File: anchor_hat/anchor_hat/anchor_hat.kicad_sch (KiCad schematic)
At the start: 25 parts, among them J1 GPIO, J2 Motor 1, J3 Motor 2, J4 24v in barrel jack, J5 24v out slip ring, J7 5v out fan right angle, U2 MCP2515-xST, U3 SN65HVD230, U4 TPS54302, Y1 12M

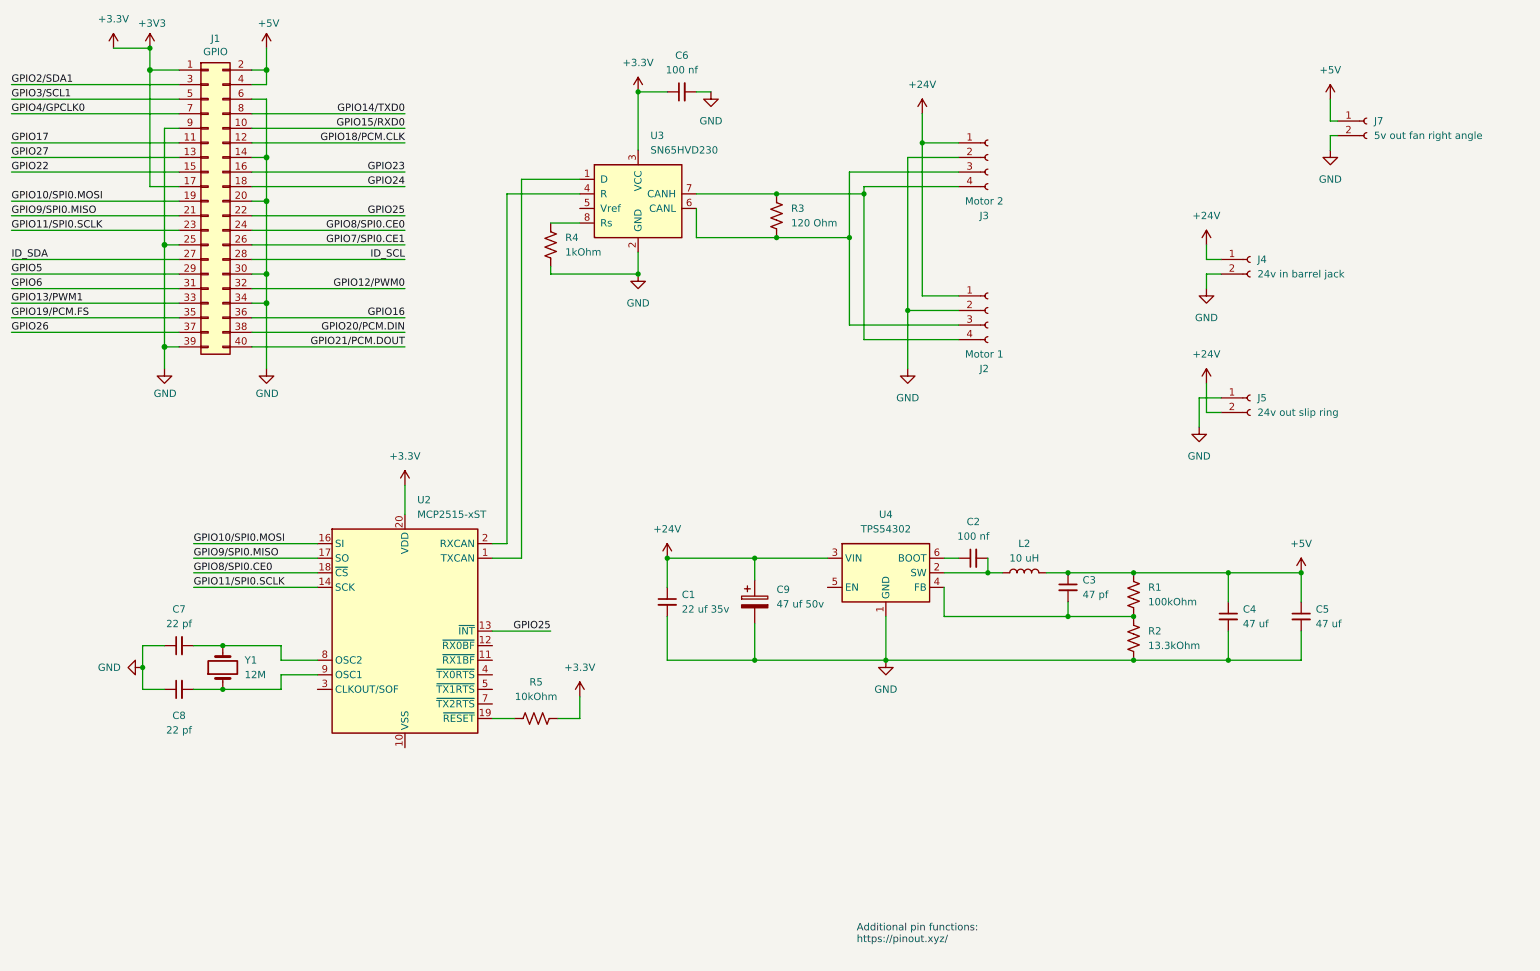
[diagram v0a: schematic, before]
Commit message: anchor hat: tvs clamps, gpio-switchable motor rail, buck uvlo, smaller crystal
TVS diodes on both sides of the buck. D1 (SMAJ26A, C49370) clamps the 24V
input, D2 (SMAJ6.0A, C364284) the 5V output; both unidirectional, cathode to
the rail. D2 is 6.0A rather than 5.0A because R1/R2 against the TPS54302's
0.596V reference put the rail at 5.08V, above an SMAJ5.0A's standoff, which
would leave it leaking continuously.

Motor rail is switchable from GPIO23. Q1 (AOD4185) is a high-side P-FET
feeding a new +24V_MOT net supplying only J2 and J3; J4, J5 and the buck stay
on +24V so the Pi keeps power. Q3 level-shifts the GPIO, R6/R7 clamp Vgs to
about -12V (the FET's limit is +/-20V, and pulling the gate to ground from 24V
would exceed it), and C10 slews the output over ~17ms so inrush into the motor
drivers does not brown out the Pi. R9 holds the switch off while the GPIO is
high-Z, and GPIO23 defaults to pull-down at boot, so the motors stay off until
firmware asserts. R10 is a DNP bleeder: without it the drivers' input caps
have no discharge path and an off-pulse does not actually power cycle them.

R11/R12 raise the buck's UVLO. U4's EN pin was floating, so the internal 4.1V
threshold let back-EMF from hand-spinning the motors boot the Pi. 560k/39k
give VSTART 18.5V and VSTOP 16.6V by the datasheet's equations 1 and 2,
leaving 7.4V of droop margin below nominal.

Y1 moves from an HC-49/U-S through-hole can to a 3225 SMD crystal (C9002).
Same 12MHz and the same 80 ohm ESR, so bit timing and oscillator startup
margin are unchanged, but it frees ~44mm2 and two drills. C7/C8 stay at 22pF:
the 18 to 20pF load change pulls the crystal about 37ppm, against the
MCP2515's 1.7% node-to-node budget.

The PCB and the BOM csv do not reflect any of this yet.

Co-Authored-By: Claude Opus 5 <noreply@anthropic.com>
Claude-Session: https://claude.ai/code/session_011o3vJPykXRkMivW79T9ddF
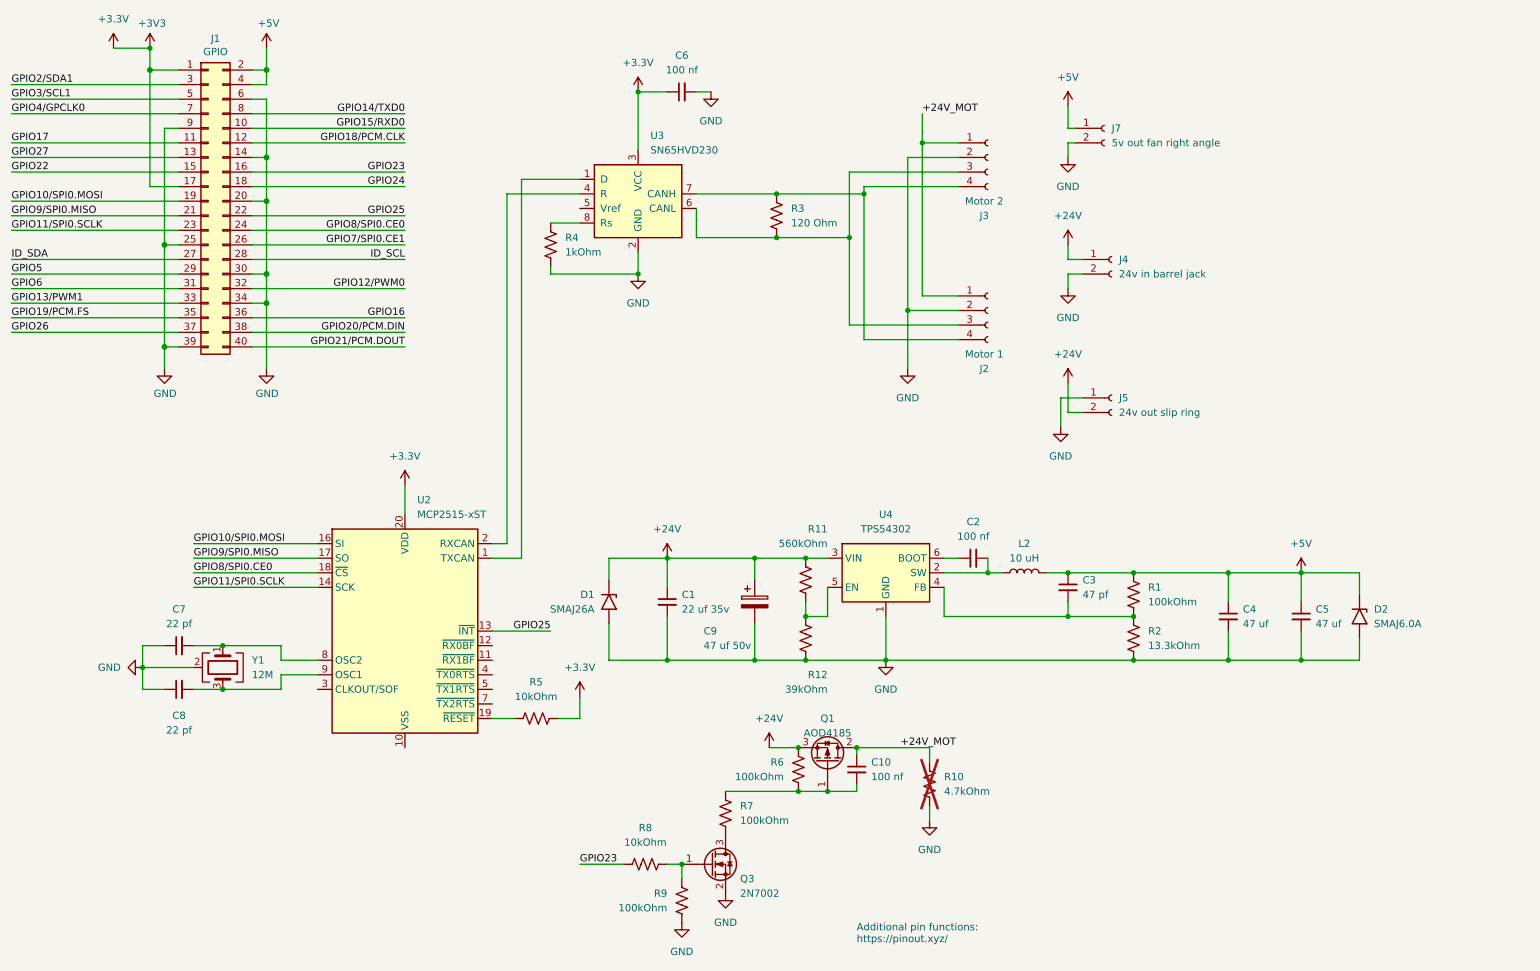
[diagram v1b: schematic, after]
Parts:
- added C10: 100 nf, Capacitor_SMD:C_0603_1608Metric, symbol Device:C_Small
- added D1: SMAJ26A, Diode_SMD:D_SMA, symbol Diode:SMAJ26A
- added D2: SMAJ6.0A, Diode_SMD:D_SMA, symbol Diode:SMAJ6.0A
- added Q1: AOD4185, Package_TO_SOT_SMD:TO-252-2, symbol Transistor_FET:Q_PMOS_GDS
- added Q3: 2N7002, Package_TO_SOT_SMD:SOT-23, symbol Transistor_FET:2N7002
- added R10: 4.7kOhm, Resistor_SMD:R_1206_3216Metric, symbol Device:R_US
- added R11: 560kOhm, Resistor_SMD:R_0603_1608Metric, symbol Device:R_US
- added R12: 39kOhm, Resistor_SMD:R_0603_1608Metric, symbol Device:R_US
- added R6, R7, R9: 100kOhm, Resistor_SMD:R_0603_1608Metric, symbol Device:R_US
- added R8: 10kOhm, Resistor_SMD:R_0603_1608Metric, symbol Device:R_US
- Y1: footprint easyeda2kicad:HC-49US_L11.5-W4.5-P4.88 -> Crystal:Crystal_SMD_3225-4Pin_3.2x2.5mm; symbol Device:Crystal -> Device:Crystal_GND24; jlc part C326537 -> C9002; manufacturer name CITIZEN -> YXC; manufacturer part number HC-49/U-S12000000ABJB -> X322512MSB4SI
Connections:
- net +24V: now also D1.1 (A1), Q1.3 (S), R11.1, R6.1; no longer J2.1 (Pin_1), J3.1 (Pin_1)
- net +5V: now also D2.1 (A1)
- net GND: now also Y1.2 (G), Y1.4 (G), D1.2 (A2), D2.2 (A2), Q3.2 (S), R10.2, R12.2, R9.2
- net GPIO23: now also R8.1
- net at C7.2, U2.8 (OSC2): now also Y1.1; no longer Y1.2
- net at C8.2, U2.9 (OSC1): now also Y1.3; no longer Y1.1
- net at U4.5 (EN): now also R11.2, R12.1
- new net: C10.2, Q1.1 (G), R6.2, R7.1
- new net: Q3.3 (D), R7.2
- new net: Q3.1 (G), R8.2, R9.1
- new net +24V_MOT: C10.1, J2.1 (Pin_1), J3.1 (Pin_1), Q1.2 (D), R10.1
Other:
- moved on the sheet: J4, J5, J7
